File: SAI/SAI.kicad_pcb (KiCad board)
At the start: 2 copper layers, 0 parts

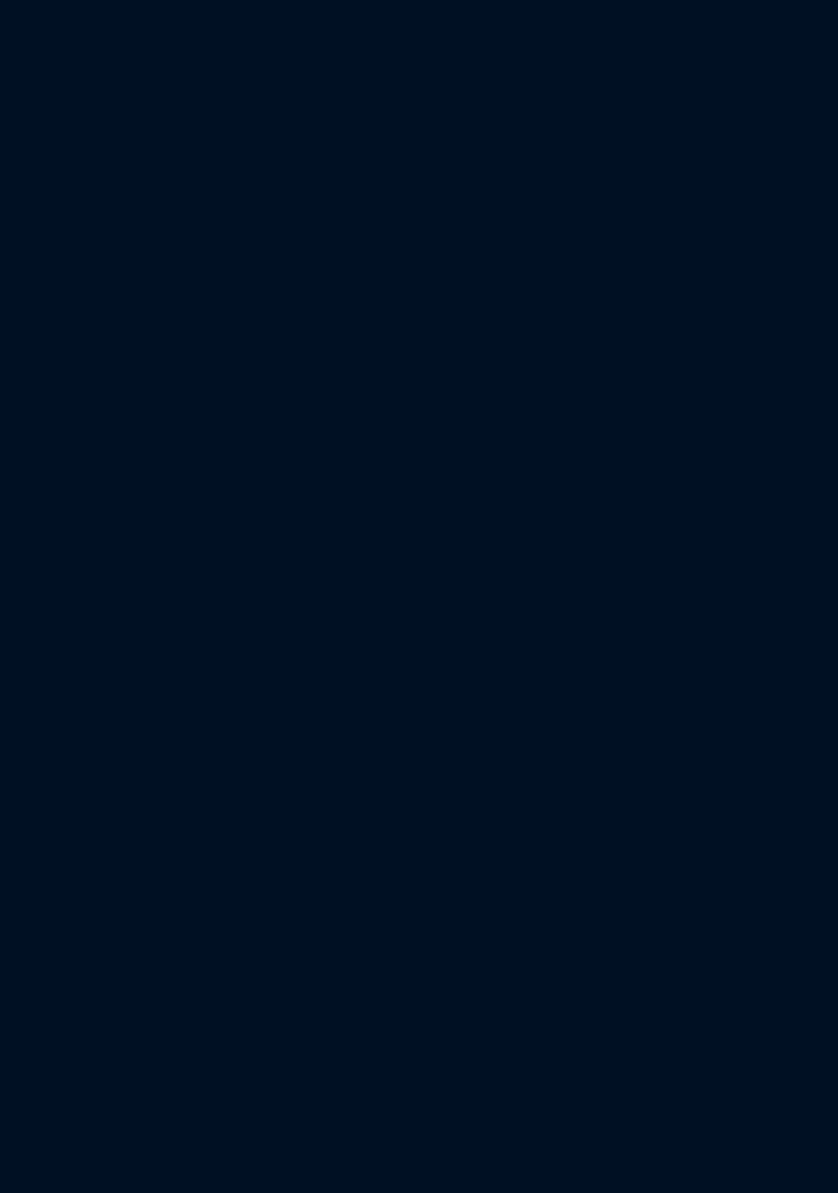
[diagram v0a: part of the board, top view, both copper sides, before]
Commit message: Added only PiPico footprint
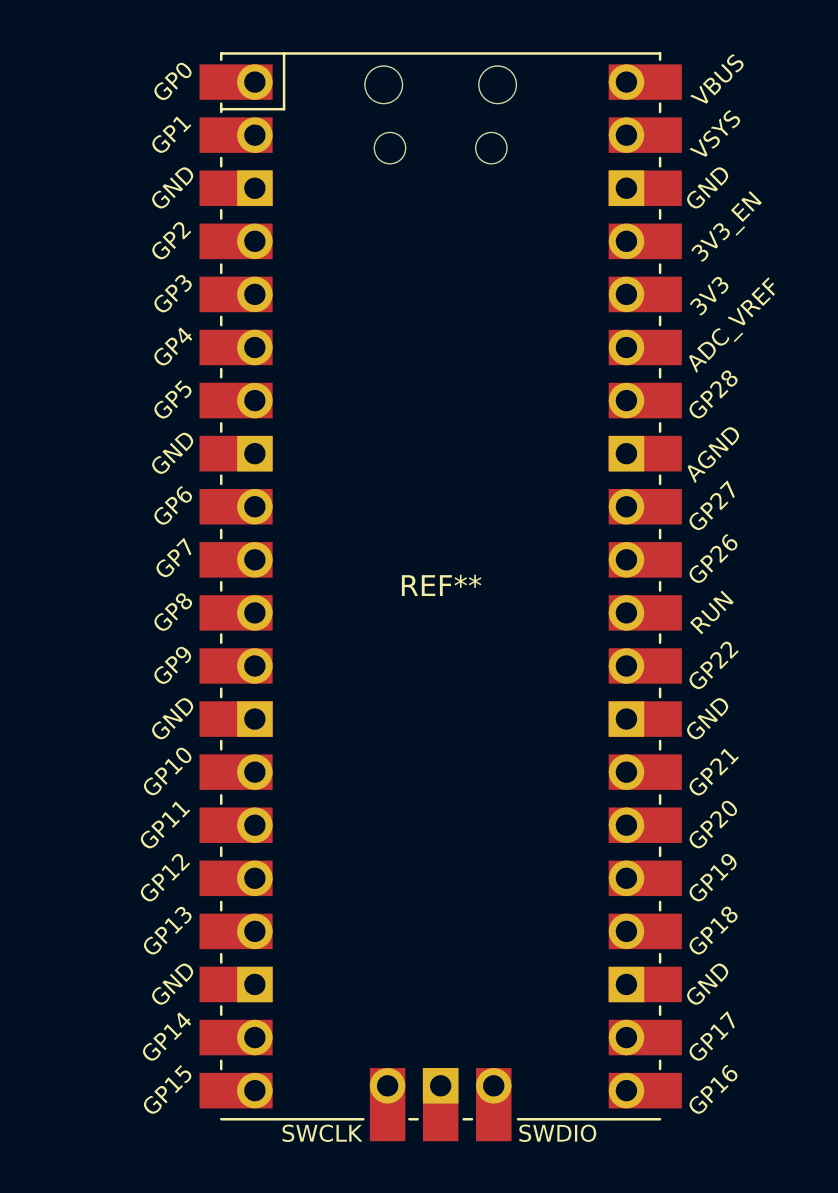
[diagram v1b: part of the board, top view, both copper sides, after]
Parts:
- added REF**: RPi_Pico_SMD_TH, MCU_RaspberryPi_and_Boards:RPi_Pico_SMD_TH, F.Cu at (157.5, 66.0)

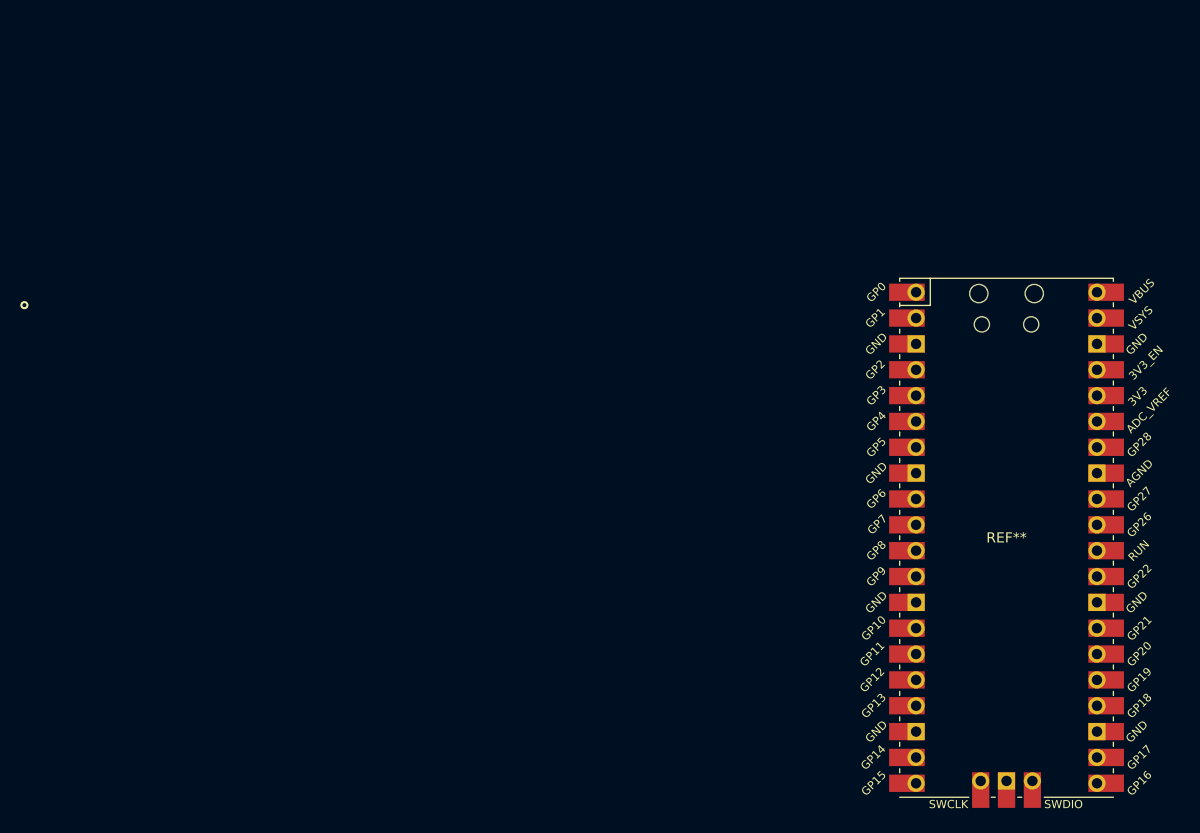
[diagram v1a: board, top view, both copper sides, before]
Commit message: Updated PI Pico schematics and footprint to map unconnected pins
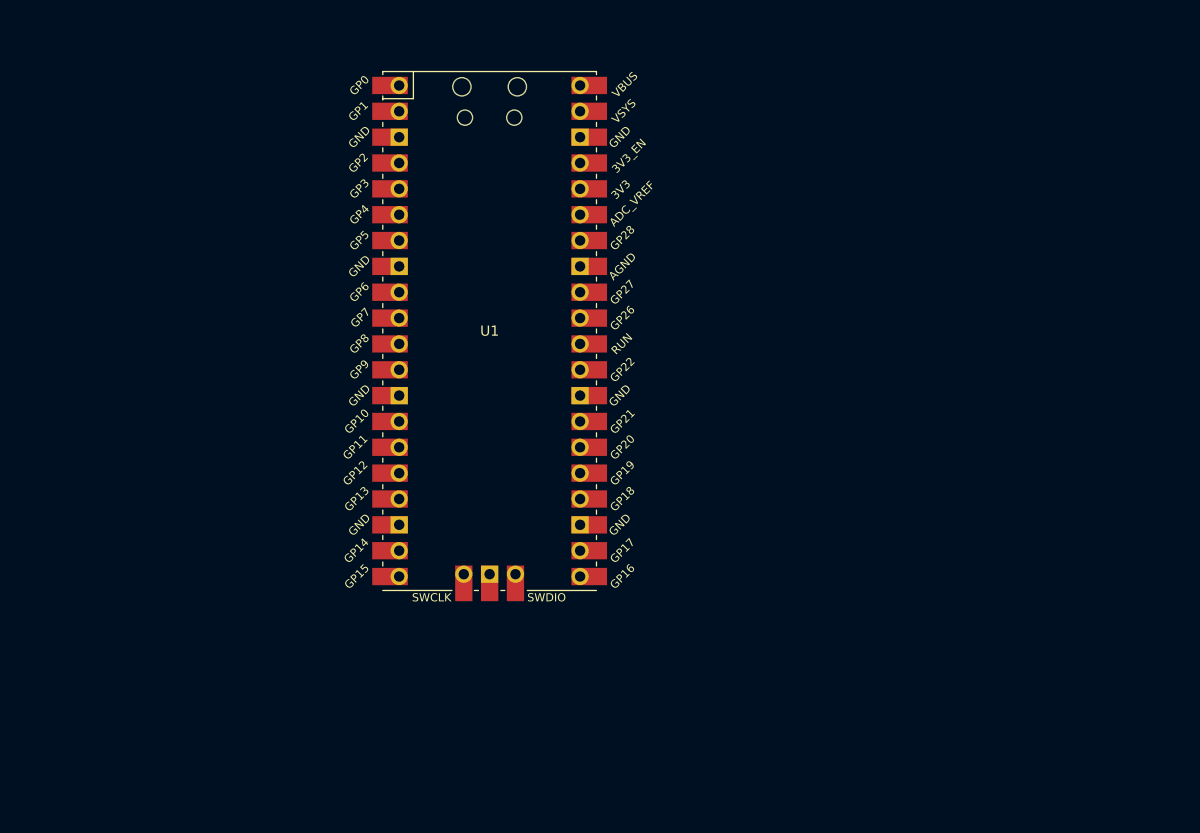
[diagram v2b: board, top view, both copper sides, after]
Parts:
- removed REF**: RPi_Pico_SMD_TH, MCU_RaspberryPi_and_Boards:RPi_Pico_SMD_TH
- added U1: Pico, MCU_RaspberryPi_and_Boards:RPi_Pico_SMD_TH, F.Cu at (106.7, 45.7)
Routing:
- net (no net): vias 1 -> 0

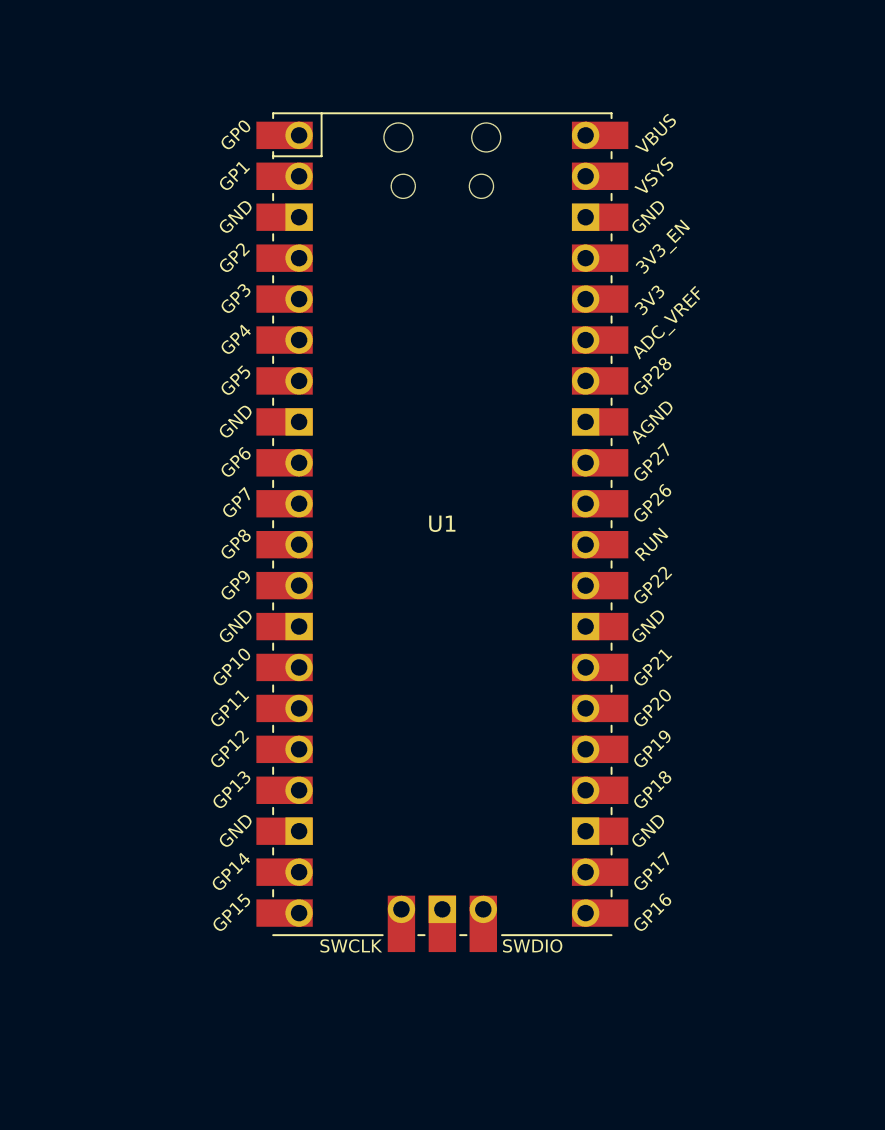
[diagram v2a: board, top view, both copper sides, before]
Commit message: Added edge cuts to Pico and now no warning or errors in DRC
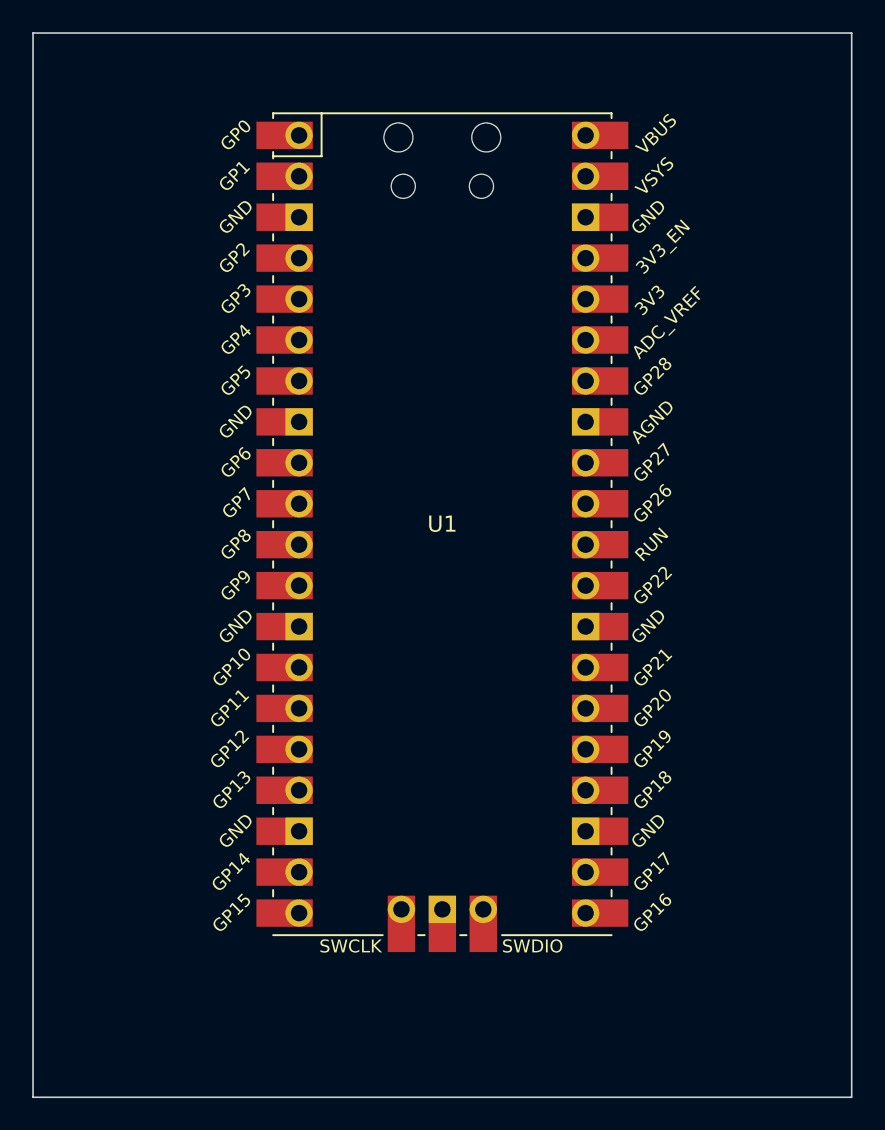
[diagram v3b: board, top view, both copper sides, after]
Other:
- board outline added: 50.8 x 66 mm
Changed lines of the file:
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@@
     )
   )
+  (gr_line (start 81.28 81.28) (end 81.28 15.24) (layer "Edge.Cuts") (width 0.1))
+  (gr_line (start 81.28 15.24) (end 132.08 15.24) (layer "Edge.Cuts") (width 0.1))
+  (gr_line (start 132.08 81.28) (end 81.28 81.28) (layer "Edge.Cuts") (width 0.1))
+  (gr_line (start 132.08 15.24) (end 132.08 81.28) (layer "Edge.Cuts") (width 0.1))
 )
